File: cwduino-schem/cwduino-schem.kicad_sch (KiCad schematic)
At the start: 5 parts, among them J1 AudioJack3

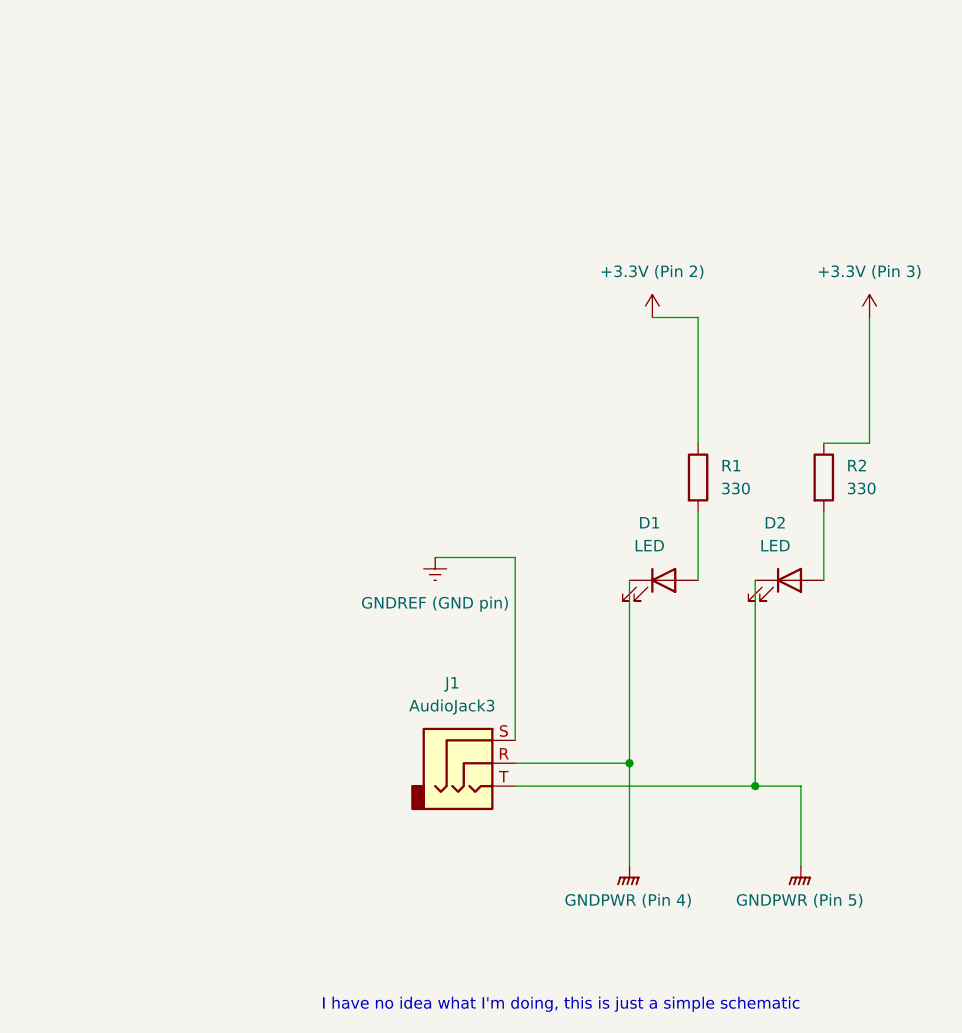
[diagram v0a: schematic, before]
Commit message: Updated schem, use Arduino Uno R3 instead of generic symbols
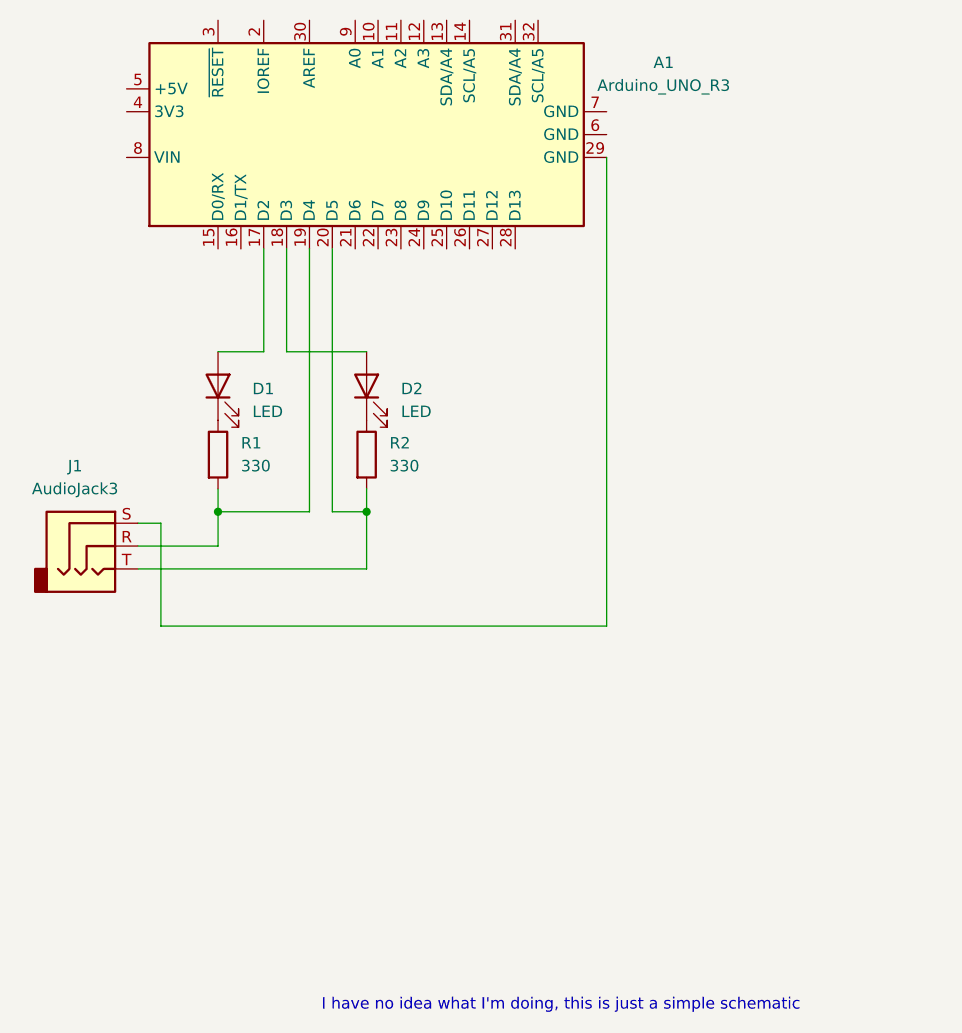
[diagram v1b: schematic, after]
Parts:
- added A1: Arduino_UNO_R3, Module:Arduino_UNO_R3, symbol MCU_Module:Arduino_UNO_R3
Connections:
- net at D2.2 (A): now also A1.18 (D3); no longer R2.2
- net at D1.2 (A): now also A1.17 (D2); no longer R1.2
- net +3.3V (Pin 2): no longer names the net of R1.1
- net +3.3V (Pin 2): now also D1.1 (K)
- net +3.3V (Pin 3): no longer names the net of R2.1
- net +3.3V (Pin 3): now also D2.1 (K)
- net GNDPWR (Pin 4): no longer names the net of J1.R
- net GNDPWR (Pin 4): now also R1.2, A1.19 (D4); no longer D1.1 (K)
- net GNDPWR (Pin 5): no longer names the net of J1.T
- net GNDPWR (Pin 5): now also R2.2, A1.20 (D5); no longer D2.1 (K)
- net GNDREF (GND pin): no longer names the net of J1.S
- net GNDREF (GND pin): now also A1.29 (GND)
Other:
- moved on the sheet: D1, D2, J1, R1, R2
